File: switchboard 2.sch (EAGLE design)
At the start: 203 parts, among them IC1 MT8816AP, IC10 Z8F2480SO, IC11 LMV321M5, IC12 74HC595D, IC14 74LVC1G125DBV, IC15 74LVC1G125DBV, IC16 LM2940, IC17 PC817S OPTO, IC2 NE5532D, IC3 TC7660-SOIC, IC4 TC7660-SOIC, IC5 FT232RL, IC6 78L05F, IC7 LD117AS33TR, IC8 SPI_MEMORY-SOIC, IC9 NE5532D, Q1 2N7002, Q2 2N7002, X1 MINI-USB-SCHIELD-32005-301

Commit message: Polarity protection changed from series diode to PMOS. Pinheaders addded to access the MCU pins directly. V+ and Vcc power supply symbols changed to +9V and +5V_AN, respectively. Spark gaps added.
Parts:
- added GAP1, GAP6: SPARK_GAP, PATSKO:SPARK_GAP
- added P_EXTRA: (no value), pinhead:PINHD-1X5
- added P_I2C: (no value), pinhead:PINHD-1X3
- added P_SPI: (no value), pinhead:PINHD-1X4
- added Q3: BSS84, transistor-small-signal:BSS84
- IC16: value LM2940 -> LM2940-9
- renumbered U$5 to GAP2, U$6 to GAP4, U$7 to GAP3, U$8 to GAP5
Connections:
- net V+ renamed +5V_AN
- removed net C_SW3: IC1.AX2, IC10.PA6/T1IN/!T1OUT!/SCL, R10.2
- removed net C_SW4: IC1.AX3, IC10.PA7/T1OUT/SDA, R11.2
- removed net VCC: C22.1, C26.1, C27.1, C30.1, C9.+, D5.A, D6.C, IC16.OUT, IC4.VCC, IC6.VI, IC7.IN, JP12.1, JP12.2, JP13.1, JP13.2, JP14.1, JP14.2, SJ6.2
- new net +9V: C22.1, C26.1, C27.1, C30.1, C9.+, D5.A, D6.A, IC16.OUT, IC4.VCC, IC6.VI, IC7.IN, JP12.1, JP12.2, JP13.1, JP13.2, JP14.1, JP14.2, SJ6.2
- new net C_SW3/SCL: IC1.AX2, IC10.PA6/T1IN/!T1OUT!/SCL, P_I2C.2, R10.2
- new net C_SW4/SDA: IC1.AX3, IC10.PA7/T1OUT/SDA, P_I2C.1, R11.2
- new net N$48: GAP6.1, P_POWER_IN.2, Q3.D
- net CS_MEM: now also P_EXTRA.2
- net CS_SHIFT: now also P_EXTRA.1
- net C_SW5: now also P_EXTRA.3
- net C_SW6: now also P_EXTRA.5
- net C_SW7: now also P_EXTRA.4
- net GND: now also GAP1.2, GAP6.2, P_I2C.3, P_SPI.4, Q3.G
- net MISO: now also P_SPI.1
- net MOSI: now also P_SPI.2
- net N$25: now also D6.C, Q3.S; no longer D6.A, P_POWER_IN.2
- net N$34: now also GAP1.1
- net SCK: now also P_SPI.3
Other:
- note added: "Buttons"
- note added: "Diode as protection against damage if Vout > Vin, providing a safe path to discharge the output caps. If LM2940 is not mounted, it should be mounted in opposite direction or replaced by a jumper."
- note added: "Generic analog input - optionally mounted if crosspoint switch MT8816 is not mounted"
- note added: "The DC blocking caps are optional and may be changed to 0R jumpers if it is guaranteed that the effects inputs and outputs doesn't have DC voltages."
- note removed: "Diode is to be mounted only if LM2940 is not mounted"
- note removed: "Generic analog input"
- note removed: "The DC blocking caps are optional and may be changed to 0R jumpers if it is guaranteed that the effects inputs and outputs have no DC voltages."
- moved on the sheet: C13, C18, C19, C20, C21, C22, C24, C25, C29, C33, C4, C5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

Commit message: Signal names changed to clarify the direction to and from external effects.
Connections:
- net EIN_1 renamed FROM_EFF_1
- net EIN_10 renamed FROM_EFF_10
- net EIN_11 renamed FROM_EFF_11
- net EIN_2 renamed FROM_EFF_2
- net EIN_3 renamed FROM_EFF_3
- net EIN_4 renamed FROM_EFF_4
- net EIN_5 renamed FROM_EFF_5
- net EIN_6 renamed FROM_EFF_6
- net EIN_7 renamed FROM_EFF_7
- net EIN_8 renamed FROM_EFF_8
- net EIN_9 renamed FROM_EFF_9
- net EOUT_1 renamed TO_EFF_1
- net EOUT_2 renamed TO_EFF_2
- net EOUT_3 renamed TO_EFF_3
- net EOUT_4 renamed TO_EFF_4
- net EOUT_5 renamed TO_EFF_5
- net EOUT_6 renamed TO_EFF_6
- net SWIN_2 renamed SW_IN_2
- net SWOUT_2-EOUT_7 renamed SWOUT_2-TO_EFF_7
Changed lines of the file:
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@@
 </segment>
 </net>
-<net name="EOUT_1" class="0">
+<net name="TO_EFF_1" class="0">
 <segment>
 <pinref part="IC1" gate="G$1" pin="Y1"/>
@@
 </segment>
 </net>
-<net name="EOUT_2" class="0">
+<net name="TO_EFF_2" class="0">
 <segment>
 <pinref part="IC1" gate="G$1" pin="Y2"/>
@@
 </segment>
 </net>
-<net name="EOUT_3" class="0">
+<net name="TO_EFF_3" class="0">
 <segment>
 <pinref part="IC1" gate="G$1" pin="Y3"/>
@@
 </segment>
 </net>
-<net name="EOUT_4" class="0">
+<net name="TO_EFF_4" class="0">
 <segment>
 <pinref part="IC1" gate="G$1" pin="Y4"/>
@@
 </segment>
 </net>
-<net name="EOUT_5" class="0">
+<net name="TO_EFF_5" class="0">
 <segment>
 <pinref part="IC1" gate="G$1" pin="Y5"/>
@@
 </segment>
 </net>
-<net name="EOUT_6" class="0">
+<net name="TO_EFF_6" class="0">
 <segment>
 <pinref part="IC1" gate="G$1" pin="Y6"/>
@@
 </segment>
 </net>
-<net name="SWOUT_2-EOUT_7" class="0">
+<net name="SWOUT_2-TO_EFF_7" class="0">
 <segment>
 <pinref part="IC1" gate="G$1" pin="Y7"/>
@@
 </segment>
 </net>
-<net name="EIN_2" class="0">
+<net name="FROM_EFF_2" class="0">
 <segment>
 <label x="-86.36" y="-360.68" size="1.778" layer="95"/>
@@
 </segment>
 </net>
-<net name="EIN_3" class="0">
+<net name="FROM_EFF_3" class="0">
 <segment>
 <label x="-86.36" y="-370.84" size="1.778" layer="95"/>
@@
 </segment>
 </net>
-<net name="EIN_4" class="0">
+<net name="FROM_EFF_4" class="0">
 <segment>
 <label x="-86.36" y="-381" size="1.778" layer="95"/>
@@
 </segment>
 </net>
-<net name="EIN_5" class="0">
+<net name="FROM_EFF_5" class="0">
 <segment>
 <label x="-86.36" y="-391.16" size="1.778" layer="95"/>
@@
 </segment>
 </net>
-<net name="EIN_6" class="0">
+<net name="FROM_EFF_6" class="0">
 <segment>
 <label x="-86.36" y="-401.32" size="1.778" layer="95"/>
@@
 </segment>
 </net>
-<net name="EIN_7" class="0">
+<net name="FROM_EFF_7" class="0">
 <segment>
 <wire x1="401.32" y1="-203.2" x2="406.4" y2="-203.2" width="0.1524" layer="91"/>
@@
 </segment>
 </net>
-<net name="EIN_8" class="0">
+<net name="FROM_EFF_8" class="0">
 <segment>
 <wire x1="401.32" y1="-200.66" x2="406.4" y2="-200.66" width="0.1524" layer="91"/>
@@
 </segment>
 </net>
-<net name="SWIN_2" class="0">
+<net name="SW_IN_2" class="0">
 <segment>
 <wire x1="50.8" y1="-241.3" x2="50.8" y2="-231.14" width="0.1524" layer="91"/>
@@
 </segment>
 </net>
-<net name="EIN_1" class="0">
+<net name="FROM_EFF_1" class="0">
 <segment>
 <label x="-86.36" y="-350.52" size="1.778" layer="95"/>
@@
 </segment>
 </net>
-<net name="EIN_9" class="0">
+<net name="FROM_EFF_9" class="0">
 <segment>
 <label x="-86.36" y="-441.96" size="1.778" layer="95"/>
@@
 </segment>
 </net>
-<net name="EIN_10" class="0">
+<net name="FROM_EFF_10" class="0">
 <segment>
 <label x="-86.36" y="-452.12" size="1.778" layer="95"/>
@@
 </segment>
 </net>
-<net name="EIN_11" class="0">
+<net name="FROM_EFF_11" class="0">
 <segment>
 <label x="-86.36" y="-462.28" size="1.778" layer="95"/>

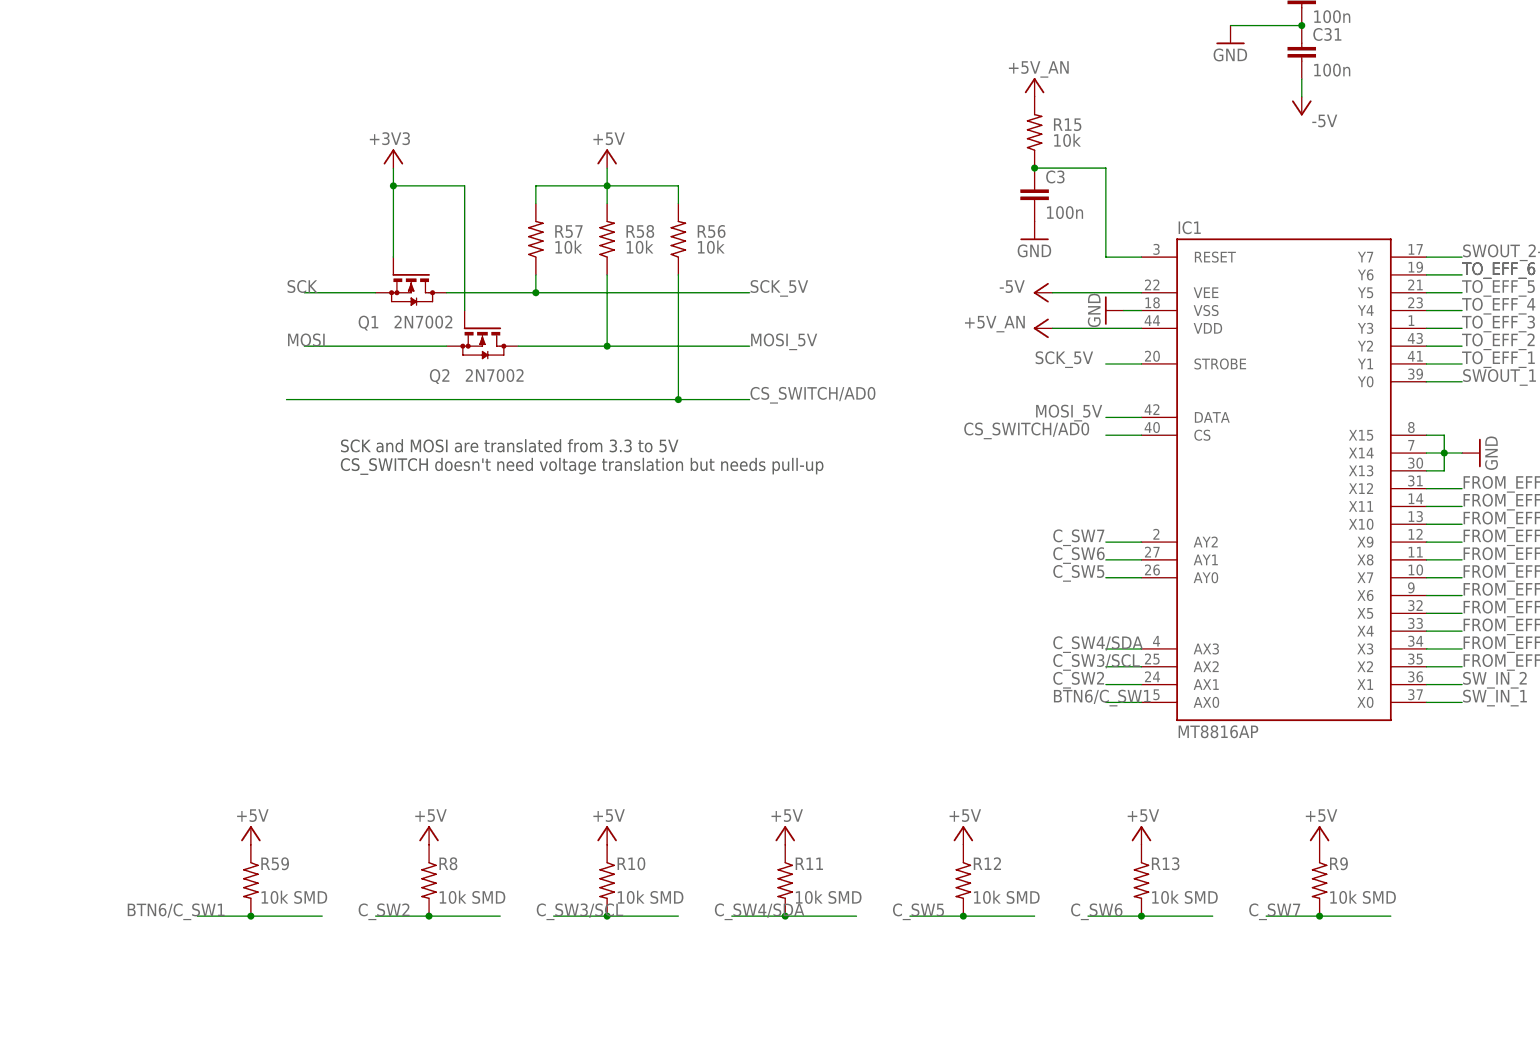
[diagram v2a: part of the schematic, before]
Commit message: Pull-ups on crosspoint address lines and voltage translator on SCK/MOSI removed.
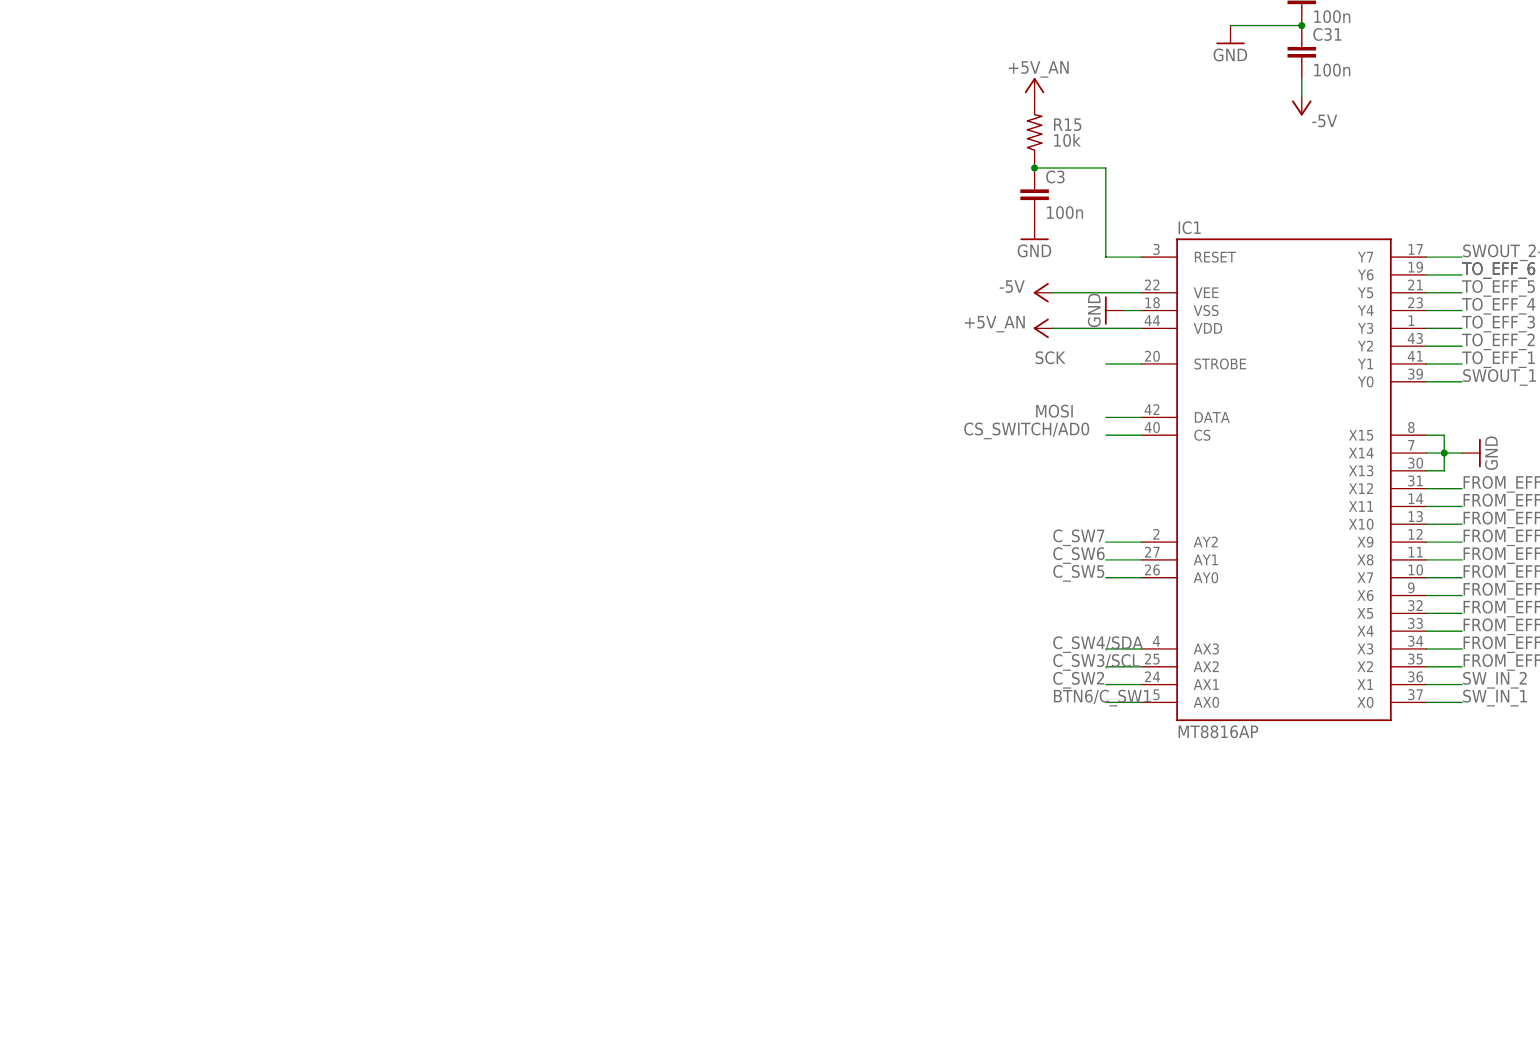
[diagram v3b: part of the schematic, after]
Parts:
- removed Q1, Q2: 2N7002, PATSKO:2N7002
- removed R10, R11, R12, R13, R59, R8, R9: 10k SMD, rcl:R-US_R0603
- removed R56, R57, R58: 10k, rcl:R-US_R0805
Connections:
- removed net MOSI_5V: IC1.DATA, Q2.D, R58.1
- removed net SCK_5V: IC1.STROBE, Q1.D, R57.1
- net +3V3: no longer Q1.G, Q2.G
- net +5V: no longer R10.1, R11.1, R12.1, R13.1, R56.2, R57.2, R58.2, R59.1, R8.1, R9.1
- net BTN6/C_SW1: no longer R59.2
- net CS_SWITCH/AD0: no longer R56.1
- net C_SW2: no longer R8.2
- net C_SW3/SCL: no longer R10.2
- net C_SW4/SDA: no longer R11.2
- net C_SW5: no longer R12.2
- net C_SW6: no longer R13.2
- net C_SW7: no longer R9.2
- net MOSI: now also IC1.DATA; no longer Q2.S
- net SCK: now also IC1.STROBE; no longer Q1.S
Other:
- note removed: "SCK and MOSI are translated from 3.3 to 5V CS_SWITCH doesn't need voltage translation but needs pull-up"

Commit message: Thru-hole pinheaders changed to SMD pinheaders.
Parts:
- removed H4: MOUNT-PAD-ROUND2.8, holes:MOUNT-PAD-ROUND2.8
- removed JP12, JP13, JP14, JP16, JP17, JP19, JP20: (no value), pinhead:PINHD-2X3
- removed JP21, JP22, JP23, JP4, JP5, JP6, JP7, JP8, JP9: (no value), pinhead:PINHD-1X2
- added JP26, JP27, JP28: (no value), pinhead-2:PINHD-2X06_2.54-SMD
- JP1, JP2, JP3: device pinhead:PINHD-1X2 -> pinhead-2:PINHD-2X03_2.54-SMD
- JP10, JP15: device pinhead:PINHD-2X3 -> pinhead-2:PINHD-2X06_2.54-SMD
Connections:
- removed net N$65: C50.2, JP20.6
- removed net N$66: C51.2, JP20.4
- removed net N$67: C52.2, JP20.2
- new net N$49: C48.2, JP28.3
- new net N$50: C49.2, JP28.5
- new net N$51: C50.2, JP28.7
- net +18V: now also JP1.5, JP1.6, JP2.5, JP2.6, JP3.5, JP3.6; no longer JP12.5, JP12.6, JP13.5, JP13.6, JP14.5, JP14.6
- net +9V: now also JP1.1, JP1.2, JP2.1, JP2.2, JP3.1, JP3.2; no longer JP12.1, JP12.2, JP13.1, JP13.2, JP14.1, JP14.2
- net BTN0: now also JP10.1, JP10.7, JP15.1, JP15.7; no longer JP23.1, JP3.1, JP6.1, JP9.1
- net BTN1: now also JP10.3, JP10.9, JP15.3, JP15.9; no longer JP2.1, JP22.1, JP5.1, JP8.1
- net BTN2: now also JP10.11, JP10.5, JP15.11, JP15.5; no longer JP1.1, JP21.1, JP4.1, JP7.1
- net BTN3: now also JP10.2, JP10.4, JP10.6; no longer JP1.2, JP2.2, JP3.2
- net BTN4: now also JP10.10, JP10.12, JP10.8; no longer JP4.2, JP5.2, JP6.2
- net BTN5: now also JP15.2, JP15.4, JP15.6; no longer JP7.2, JP8.2, JP9.2
- net BTN6/C_SW1: now also JP15.10, JP15.12, JP15.8; no longer JP21.2, JP22.2, JP23.2
- net GND: now also JP1.3, JP1.4, JP2.3, JP2.4, JP26.10, JP26.12, JP26.2, JP26.4, JP26.6, JP26.8, JP27.10, JP27.12, JP27.2, JP27.4, JP27.6, JP27.8, JP28.10, JP28.12, JP28.2, JP28.4, JP28.6, JP28.8, JP3.3, JP3.4; no longer JP10.1, JP10.3, JP10.5, JP12.3, JP12.4, JP13.3, JP13.4, JP14.3, JP14.4, JP15.1, JP15.3, JP15.5, JP16.1, JP16.3, JP16.5, JP17.1, JP17.3, JP17.5, JP19.1, JP19.3, JP19.5, JP20.1, JP20.3, JP20.5
- net N$12: now also JP27.1; no longer JP10.6
- net N$15: now also JP27.3; no longer JP10.4
- net N$16: now also JP27.5; no longer JP10.2
- net N$17: now also JP27.7; no longer JP15.6
- net N$18: now also JP27.9; no longer JP15.4
- net N$19: now also JP27.11; no longer JP15.2
- net N$21: now also JP26.1; no longer JP16.6
- net N$32: now also JP26.3; no longer JP16.4
- net N$52: now also JP26.5; no longer JP16.2
- net N$53: now also JP26.7; no longer JP17.6
- net N$59: now also JP26.9; no longer JP17.4
- net N$62: now also JP26.11; no longer JP17.2
- net N$63: now also C51.2, JP28.9; no longer C48.2, JP19.4
- net N$64: now also C52.2, JP28.11; no longer C49.2, JP19.2
- net N$9: now also JP28.1; no longer JP19.6
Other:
- note added: "BTN0 to BTN2 Configure as open-drain outputs with pull-ups"
- note added: "BTN3 to BTN6 Configure as inputs with pull-ups"
- note removed: "Configure as inputs with pull-ups"
- note removed: "Configure as open-drain outputs with pull-ups"

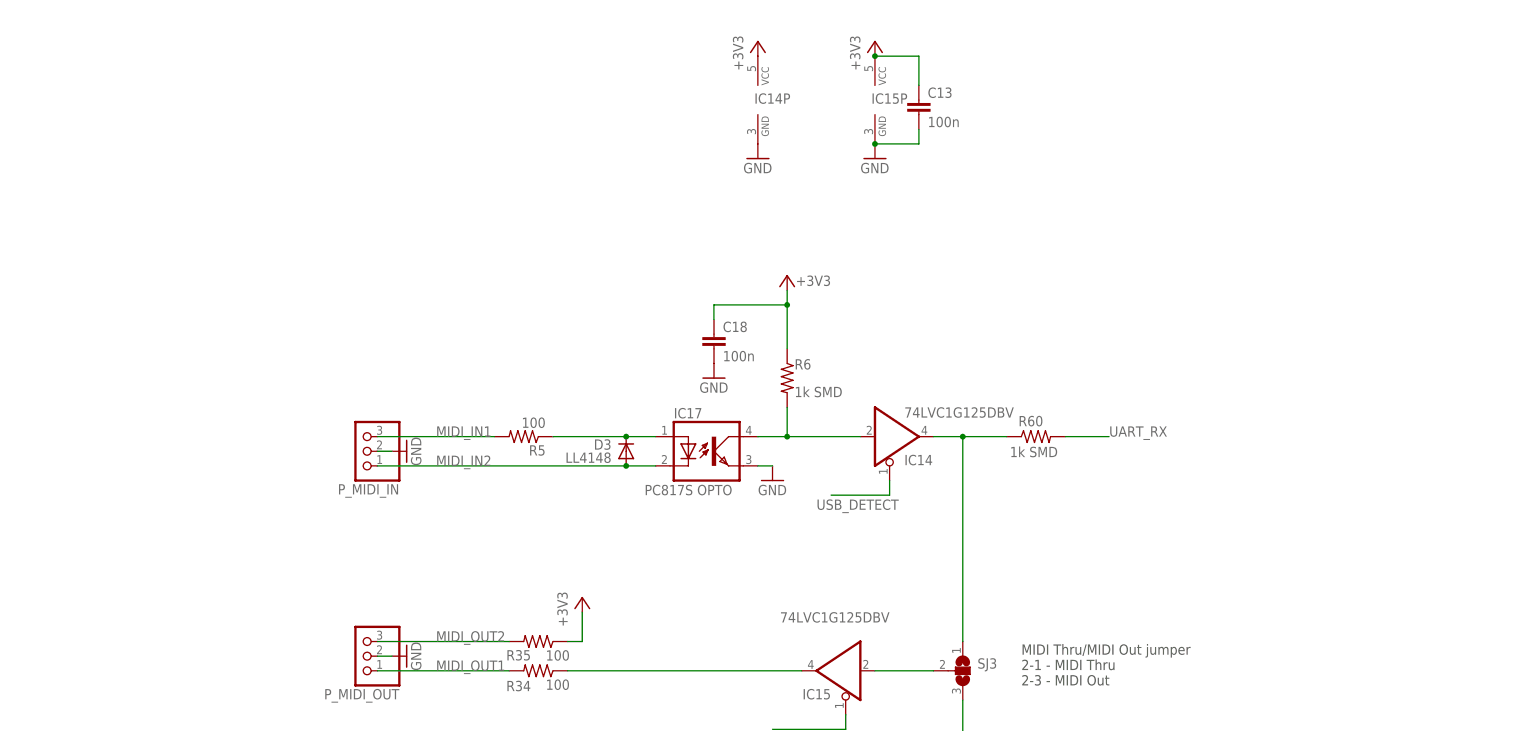
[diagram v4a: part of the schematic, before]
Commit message: RC filter added to MIDI 3V3 supply. GND1 added to connect the MIDI In cable shield.
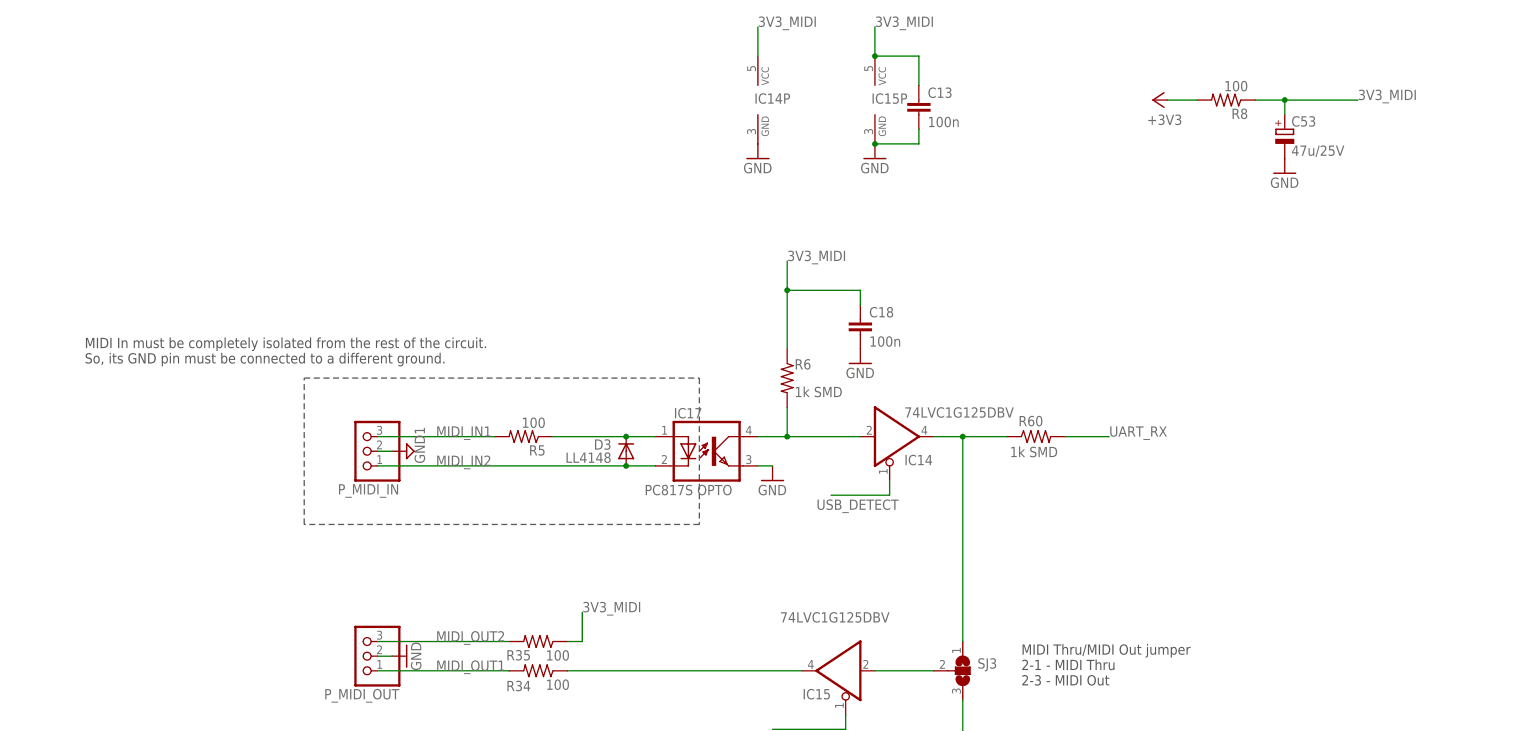
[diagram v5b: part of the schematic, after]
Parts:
- added C53: 47u/25V, PATSKO:CAP_POLALUM-TANT
- added R8: 100, rcl:R-US_R0603
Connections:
- new net 3V3_MIDI: C13.1, C18.1, C53.+, IC14P.VCC, IC15P.VCC, R35.1, R6.1, R8.1
- new net GND1: P_MIDI_IN.2
- net +3V3: now also R8.2; no longer C13.1, C18.1, IC14P.VCC, IC15P.VCC, R35.1, R6.1
- net GND: now also C53.-; no longer P_MIDI_IN.2
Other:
- note added: "MIDI In must be completely isolated from the rest of the circuit. So, its GND pin must be connected to a different ground."
- moved on the sheet: C18
